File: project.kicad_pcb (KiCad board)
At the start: 2 copper layers, 3 parts, among them J1 7S_CSE_IAS, J2 7S_HDG

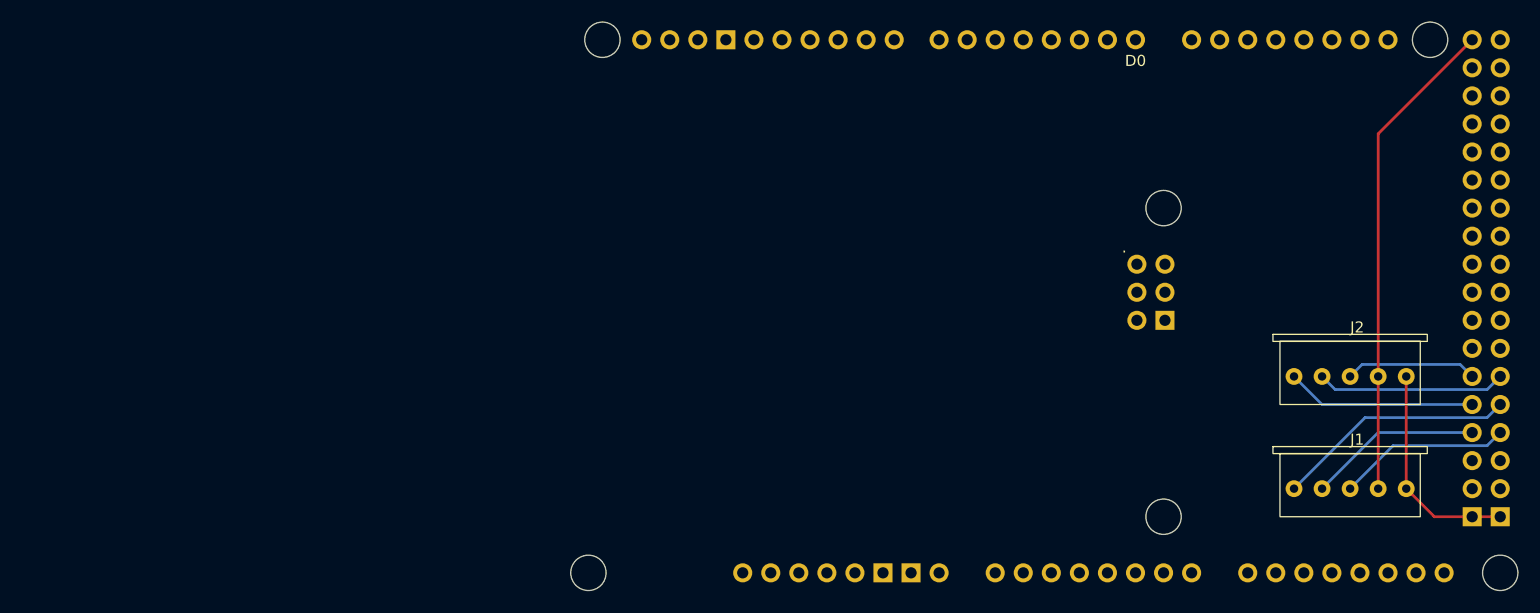
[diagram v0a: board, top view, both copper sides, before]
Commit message: feat: route south part of bottom layer
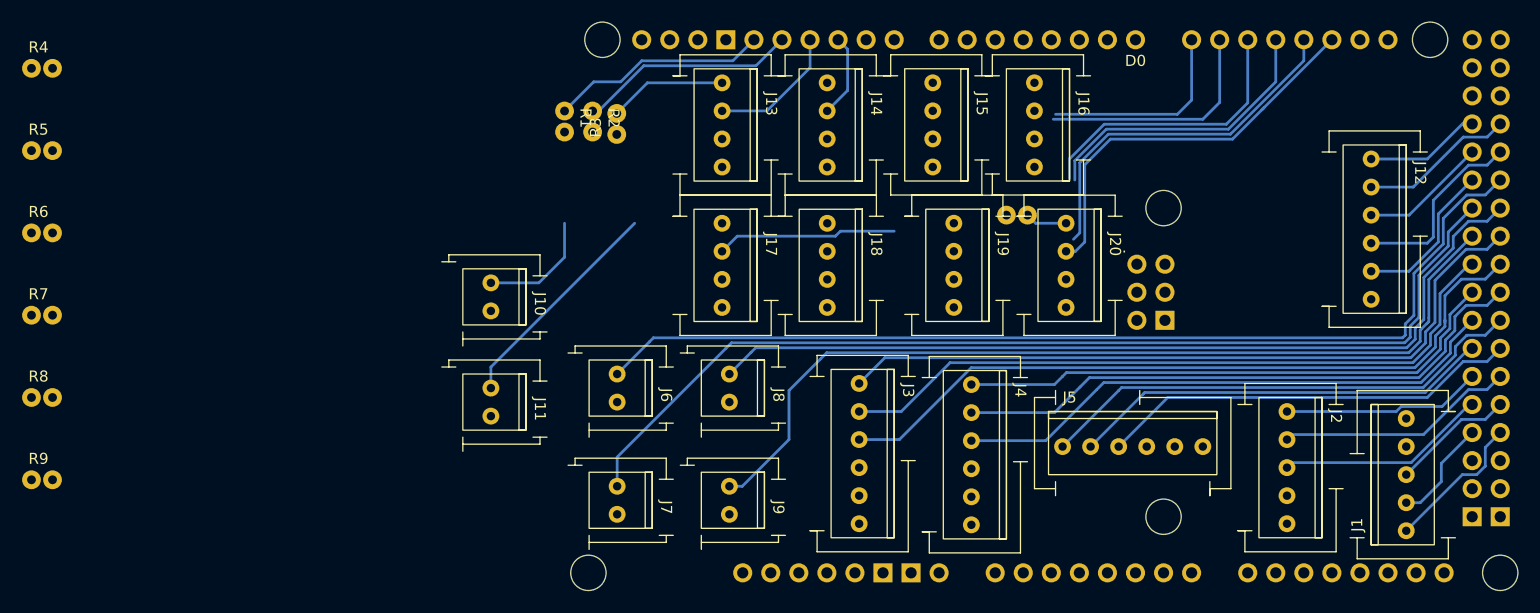
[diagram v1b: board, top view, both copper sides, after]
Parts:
- added J10: LED_CPT_FD, footprint_library:TE Conn - 640456-2, F.Cu at (104.5, 88.0)
- added J11: LED_AT, footprint_library:TE Conn - 640456-2, F.Cu at (104.5, 97.6)
- added J12: NPS_BANK_ANGLE, footprint_library:TE Conn - 640456-6, F.Cu at (184.2, 76.8)
- added J13: KD_N1, footprint_library:TE Conn - 640456-4, F.Cu at (125.4, 69.9)
- added J14: KD_SPD, footprint_library:TE Conn - 640456-4, F.Cu at (134.9, 69.9)
- added J15: KD_LVL_CHG, footprint_library:TE Conn - 640456-4, F.Cu at (144.5, 69.9)
- added J16: KD_VNAV, footprint_library:TE Conn - 640456-4, F.Cu at (153.7, 69.9)
- added J17: KD_HDG_SEL, footprint_library:TE Conn - 640456-4, F.Cu at (125.4, 82.7)
- added J18: KD_APP, footprint_library:TE Conn - 640456-4, F.Cu at (134.9, 82.7)
- added J19: KD_VOR_LOC, footprint_library:TE Conn - 640456-4, F.Cu at (146.4, 82.7)
- added J20: KD_LNAV, footprint_library:TE Conn - 640456-4, F.Cu at (156.5, 82.7)
- added J3: ENC_HDG, footprint_library:TE Conn - 640456-6, F.Cu at (137.8, 97.2)
- added J4: ENC_IAS, footprint_library:TE Conn - 640456-6, F.Cu at (148.0, 97.3)
- added J5: ENC_CSE, footprint_library:TE Conn - 640456-6, F.Cu at (157.5, 109.2)
- added J6: SEL_CPT_FD, footprint_library:TE Conn - 640456-2, F.Cu at (115.9, 96.3)
- added J7: SEL_AT, footprint_library:TE Conn - 640456-2, F.Cu at (115.9, 106.5)
- added J8: PSH_CO, footprint_library:TE Conn - 640456-2, F.Cu at (126.0, 96.3)
- added J9: PSH_SPD_INTV, footprint_library:TE Conn - 640456-2, F.Cu at (126.0, 106.5)
- added R1: 100R, footprint_library:xs resistor PT, F.Cu at (112.4, 72.5)
- added R10: 100R, footprint_library:xs resistor PT, F.Cu at (152.4, 87.0)
- added R2: 100R, footprint_library:xs resistor PT, F.Cu at (114.9, 72.5)
- added R3: 100R, footprint_library:xs resistor PT, F.Cu at (122.2, 79.7)
- added R4: 100R, footprint_library:xs resistor PT, F.Cu at (64.1, 73.7)
- added R5: 100R, footprint_library:xs resistor PT, F.Cu at (64.1, 81.2)
- added R6: 100R, footprint_library:xs resistor PT, F.Cu at (64.1, 88.6)
- added R7: 100R, footprint_library:xs resistor PT, F.Cu at (64.1, 96.1)
- added R8: 100R, footprint_library:xs resistor PT, F.Cu at (64.1, 103.5)
- added R9: 100R, footprint_library:xs resistor PT, F.Cu at (64.1, 111.0)
- moved J1 16.7 mm to (194.9, 115.6), turned to 90 degrees
- moved J2 3.70 mm to (176.5, 99.7), turned to -90 degrees
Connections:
- A1 pad D10: unconnected-(A1-PadD10) -> KD2
- A1 pad D11: unconnected-(A1-PadD11) -> KD1
- A1 pad D12: unconnected-(A1-PadD12) -> LED2
- A1 pad D13: unconnected-(A1-PadD13) -> LED1
- A1 pad D14: unconnected-(A1-D14/TX3-PadD14) -> KD3
- A1 pad D15: unconnected-(A1-D15/RX3-PadD15) -> KD4
- A1 pad D16: unconnected-(A1-D16/TX2-PadD16) -> KD5
- A1 pad D17: unconnected-(A1-D17/RX2-PadD17) -> KD6
- A1 pad D18: unconnected-(A1-D18/TX1-PadD18) -> KD7
- A1 pad D19: unconnected-(A1-D19/RX1-PadD19) -> KD8
- A1 pad D2: unconnected-(A1-D2_INT0-PadD2) -> Net-(A1-D2_INT0)
- A1 pad D26: unconnected-(A1-PadD26) -> Net-(A1-PadD26)
- A1 pad D27: unconnected-(A1-PadD27) -> Net-(A1-PadD27)
- A1 pad D28: unconnected-(A1-PadD28) -> Net-(A1-PadD28)
- A1 pad D29: unconnected-(A1-PadD29) -> Net-(A1-PadD29)
- A1 pad D3: unconnected-(A1-D3_INT1-PadD3) -> Net-(A1-D3_INT1)
- A1 pad D30: unconnected-(A1-PadD30) -> Net-(A1-PadD30)
- A1 pad D31: unconnected-(A1-PadD31) -> Net-(A1-PadD31)
- A1 pad D32: unconnected-(A1-PadD32) -> Net-(A1-PadD32)
- A1 pad D33: unconnected-(A1-PadD33) -> Net-(A1-PadD33)
- A1 pad D34: unconnected-(A1-PadD34) -> Net-(A1-PadD34)
- A1 pad D35: unconnected-(A1-PadD35) -> Net-(A1-PadD35)
- A1 pad D36: unconnected-(A1-PadD36) -> Net-(A1-PadD36)
- A1 pad D37: unconnected-(A1-PadD37) -> Net-(A1-PadD37)
- A1 pad D38: unconnected-(A1-PadD38) -> Net-(A1-PadD38)
- A1 pad D39: unconnected-(A1-PadD39) -> Net-(A1-PadD39)
- A1 pad D4: unconnected-(A1-PadD4) -> Net-(A1-PadD4)
- A1 pad D40: unconnected-(A1-PadD40) -> Net-(A1-PadD40)
- A1 pad D41: unconnected-(A1-PadD41) -> Net-(A1-PadD41)
- A1 pad D42: unconnected-(A1-PadD42) -> Net-(A1-PadD42)
- A1 pad D43: unconnected-(A1-PadD43) -> Net-(A1-PadD43)
- A1 pad D5: unconnected-(A1-PadD5) -> Net-(A1-PadD5)
- A1 pad D6: unconnected-(A1-PadD6) -> Net-(A1-PadD6)
- A1 pad D7: unconnected-(A1-PadD7) -> Net-(A1-PadD7)
- A1 pad D8: unconnected-(A1-PadD8) -> Net-(A1-PadD8)
- A1 pad D9: unconnected-(A1-PadD9) -> Net-(A1-PadD9)
- J1 pad 1: Net-(A1-PadD47) -> Net-(A1-PadD49)
- J1 pad 3: Net-(A1-PadD49) -> Net-(A1-PadD47)
- J2 pad 1: Net-(A1-PadD46) -> Net-(A1-PadD44)
- J2 pad 3: Net-(A1-PadD44) -> Net-(A1-PadD46)
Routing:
- net Net-(A1-PadD32): track 0.00 -> 92.9 mm
- net Net-(A1-PadD31): track 0.00 -> 91.4 mm
- net Net-(A1-PadD34): track 0.00 -> 82.2 mm
- net Net-(A1-PadD33): track 0.00 -> 79.4 mm
- net Net-(A1-PadD37): track 0.00 -> 67.1 mm
- net Net-(A1-PadD35): track 0.00 -> 66.4 mm
- net Net-(A1-PadD36): track 0.00 -> 63.2 mm
- net Net-(A1-PadD39): track 0.00 -> 53.7 mm
- net Net-(A1-PadD40): track 0.00 -> 50.8 mm
- net Net-(A1-PadD38): track 0.00 -> 50.1 mm
- net Net-(A1-PadD41): track 0.00 -> 44.8 mm
- net VCC: track 44.2 -> 0.00 mm
- net KD5: track 0.00 -> 42.0 mm
- net Net-(A1-PadD43): track 0.00 -> 38.2 mm
- net Net-(A1-PadD42): track 0.00 -> 38.2 mm
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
